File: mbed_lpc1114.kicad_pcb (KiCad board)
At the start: 2 copper layers, 74.9 x 53.3 mm, 32 parts, among them J1 CONN_01X08, J2 CONN_01X06, J3 CONN_01X08, J4 CONN_01X10, J5 USB_B, U1 lpc1114fn28, U2 PL2303SA, U3 7803, U4 PushSwitch, U5 PushSwitch

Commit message: 完成！
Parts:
- R8: footprint Resistors_THT:R_Axial_DIN0207_L6.3mm_D2.5mm_P15.24mm_Horizontal -> Resistors_THT:R_Axial_DIN0207_L6.3mm_D2.5mm_P10.16mm_Horizontal
- moved C6 4.55 mm to (85.1, 68.6)
- moved U1 4.26 mm to (69.8, 87.0)
- moved D1 3.70 mm to (101.0, 90.8), turned to 0 degrees
- moved C7 2.69 mm to (85.7, 90.8)
- moved REF** 1.42 mm to (101.6, 66.7)
- moved R8 0.90 mm to (88.3, 90.8)
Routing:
- net +3V3: track 79.6 -> 143.4 mm, vias 4 -> 6
- net Net-(J3-Pad7): track 28.0 -> 91.5 mm, vias 1 -> 4
- net Net-(J3-Pad8): track 73.0 -> 83.2 mm, vias 4 -> 6
- net Net-(J2-Pad6): track 100.8 -> 110.6 mm
- net Net-(J4-Pad5): track 48.2 -> 54.4 mm
- net Net-(D1-Pad2): track 52.5 -> 57.4 mm
- net Net-(J2-Pad5): track 80.9 -> 85.6 mm
- net Net-(C9-Pad1): track 60.4 -> 64.8 mm
- net +5V: track 71.1 -> 75.4 mm
- net Net-(J2-Pad3): track 16.8 -> 13.3 mm
- net Net-(J2-Pad1): track 23.3 -> 19.8 mm
- net Net-(J4-Pad7): track 39.5 -> 42.9 mm
- net Net-(J3-Pad6): track 18.3 -> 21.8 mm
- net Net-(J3-Pad1): track 52.2 -> 55.5 mm
- net GND: track 240.3 -> 237.4 mm, vias 2 -> 4
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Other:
- board size 74.9 x 53.3 mm -> 77.5 x 53.3 mm
- net class Default: clearance 0.2 -> 0.4
- rule trace_clearance: 0.2 -> 0.4

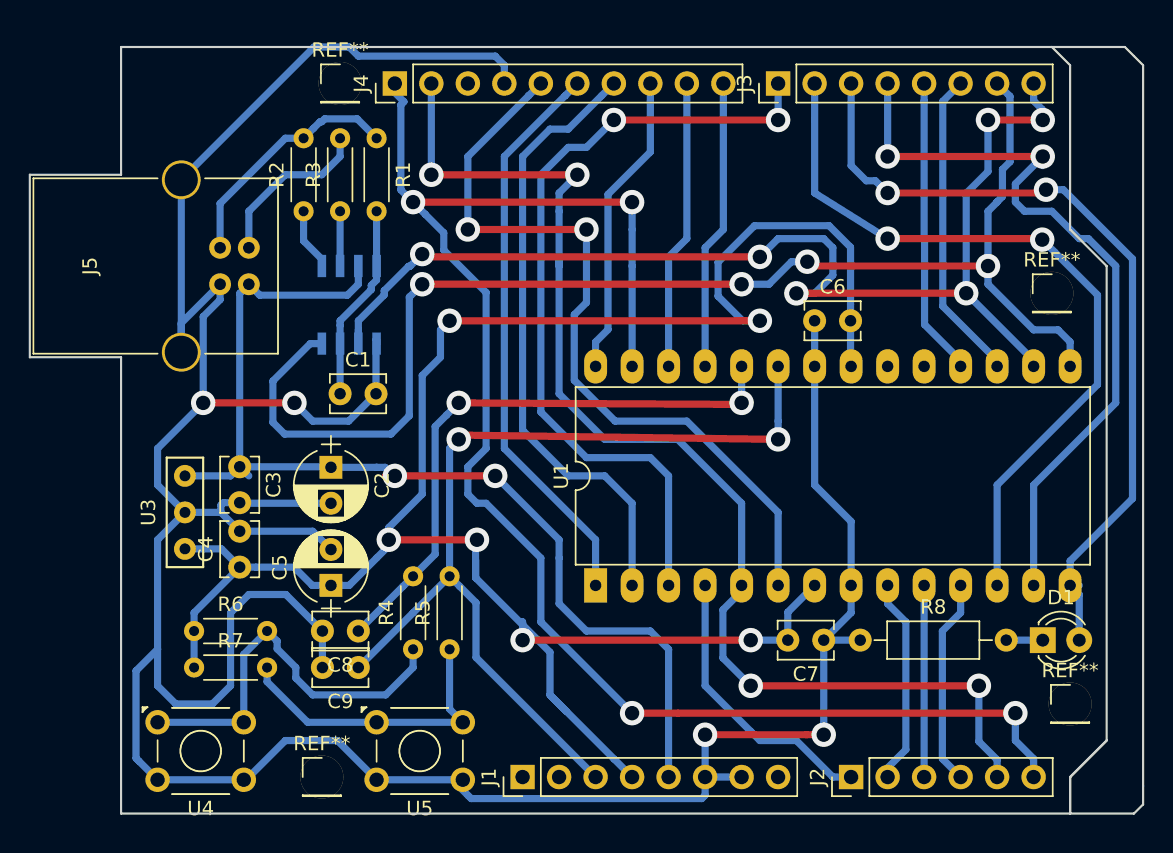
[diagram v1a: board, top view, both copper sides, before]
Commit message: ベタグラウンドを追加
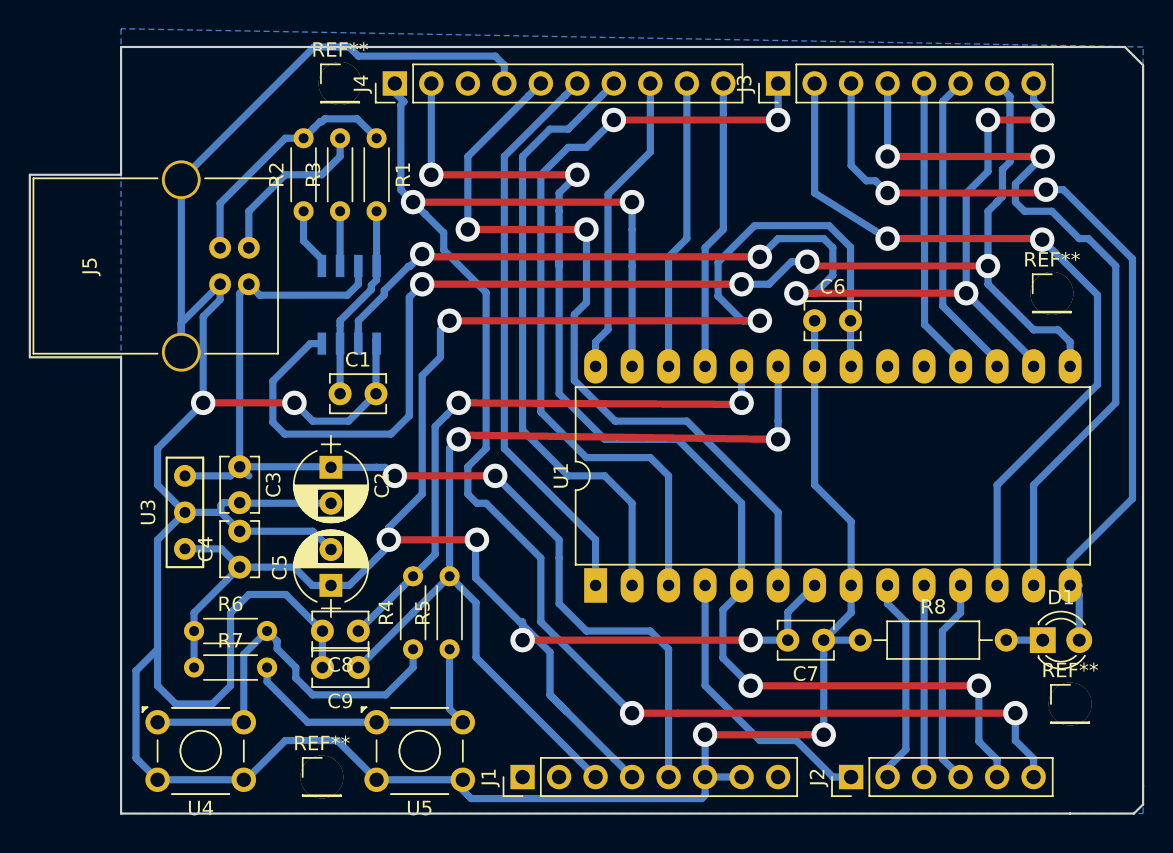
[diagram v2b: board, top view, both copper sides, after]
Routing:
- added copper zone on B.Cu, net GND
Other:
- outline, holes or cut-outs redrawn
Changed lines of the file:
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@@
     (links 82)
     (no_connects 0)
-    (area 30.404999 49.454999 108.025001 102.945001)
+    (area 30.044999 46.836666 121.515 113.19)
     (thickness 1.6)
-    (drawings 24)
+    (drawings 16)
     (tracks 480)
     (zones 0)
@@
       (effects (font (size 1 1) (thickness 0.15)))
     )
-    (fp_text value CONN_01X06 (at 0 15.03 90) (layer F.Fab)
+    (fp_text value CONN_01X06 (at 5.08 35.56 90) (layer F.Fab)
       (effects (font (size 1 1) (thickness 0.15)))
     )
@@
   (gr_line (start 106.68 49.53) (end 107.315 50.165) (layer Edge.Cuts) (width 0.15))
   (gr_line (start 101.6 49.53) (end 106.68 49.53) (layer Edge.Cuts) (width 0.15))
-  (gr_line (start 102.87 100.33) (end 105.41 97.79) (angle 90) (layer Edge.Cuts) (width 0.15))
-  (gr_line (start 102.87 102.87) (end 102.87 100.33) (angle 90) (layer Edge.Cuts) (width 0.15))
   (gr_line (start 36.83 102.87) (end 102.87 102.87) (angle 90) (layer Edge.Cuts) (width 0.15))
   (gr_line (start 36.83 71.12) (end 36.83 102.87) (angle 90) (layer Edge.Cuts) (width 0.15))
@@
   (gr_line (start 36.83 49.53) (end 36.83 58.42) (angle 90) (layer Edge.Cuts) (width 0.15))
   (gr_line (start 101.6 49.53) (end 36.83 49.53) (angle 90) (layer Edge.Cuts) (width 0.15))
-  (gr_line (start 102.87 50.8) (end 101.6 49.53) (angle 90) (layer Edge.Cuts) (width 0.15))
-  (gr_line (start 102.87 62.23) (end 102.87 50.8) (angle 90) (layer Edge.Cuts) (width 0.15))
-  (gr_line (start 105.41 64.77) (end 102.87 62.23) (angle 90) (layer Edge.Cuts) (width 0.15))
-  (gr_line (start 105.41 97.79) (end 105.41 64.77) (angle 90) (layer Edge.Cuts) (width 0.15))
-  (gr_line (start 102.87 100.33) (end 105.41 97.79) (angle 90) (layer Edge.Cuts) (width 0.15))
-  (gr_line (start 102.87 102.87) (end 102.87 100.33) (angle 90) (layer Edge.Cuts) (width 0.15))
   (segment (start 50.26 49.53) (end 52.705 49.53) (width 0.5) (layer B.Cu) (net 1))
   (segment (start 52.705 49.53) (end 53.34 50.165) (width 0.5) (layer B.Cu) (net 1))
@@
   (segment (start 69.85 71.755) (end 69.85 70.055) (width 0.5) (layer B.Cu) (net 33))
   (segment (start 73.66 53.272081) (end 73.66 52.07) (width 0.5) (layer B.Cu) (net 33))
+  (zone (net 1) (net_name GND) (layer B.Cu) (hatch edge 0.508)
+    (connect_pads (clearance 0.508))
+    (min_thickness 0.254)
+    (fill yes (arc_segments 16) (thermal_gap 0.508) (thermal_bridge_width 0.508))
+    (polygon
+      (pts
+        (xy 36.83 49.53) (xy 36.83 102.87) (xy 107.95 102.87) (xy 107.95 49.53) (xy 36.83 48.26)
+      )
+    )
+  )
 )
